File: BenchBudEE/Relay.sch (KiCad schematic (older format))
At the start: 10 parts

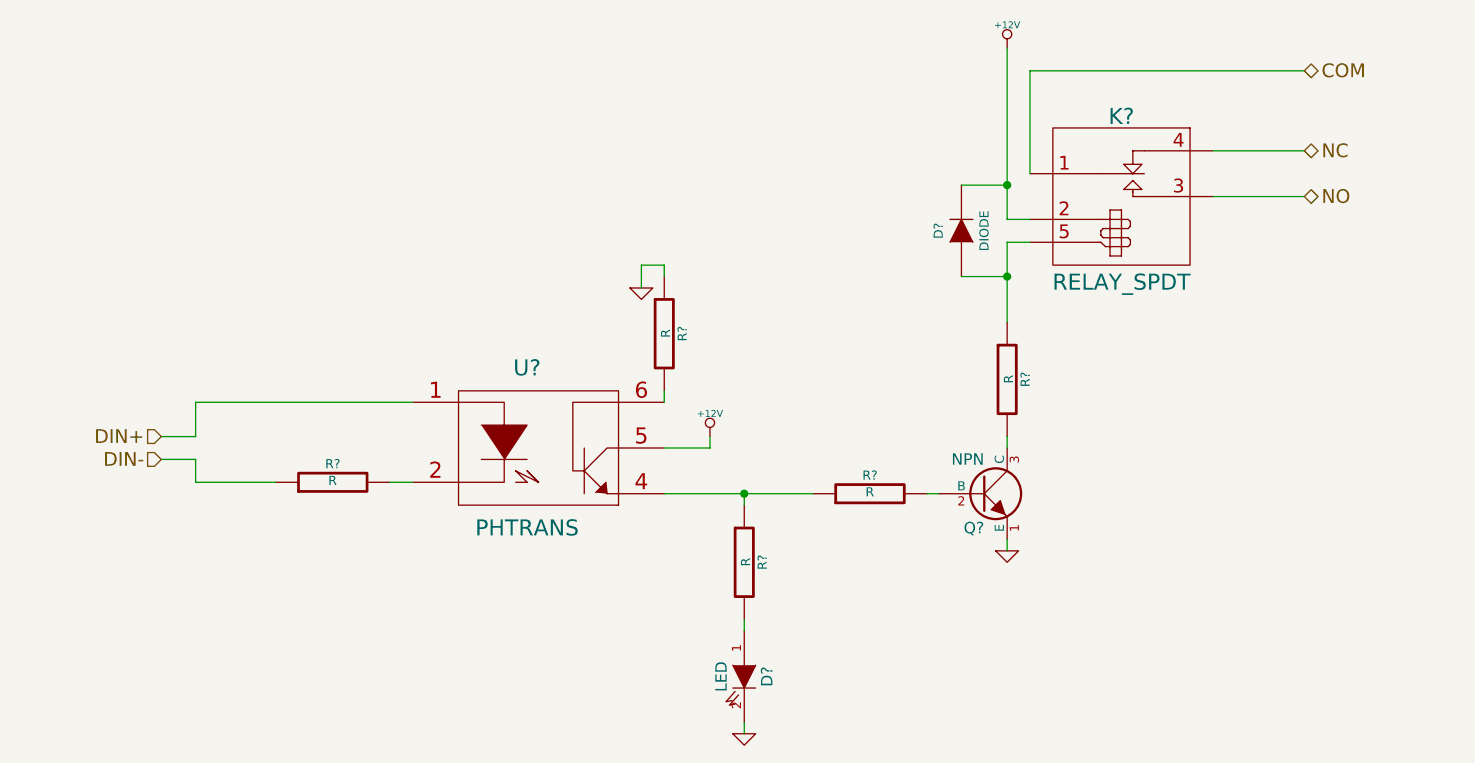
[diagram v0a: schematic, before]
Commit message: Completing schematics from week 3 videos.
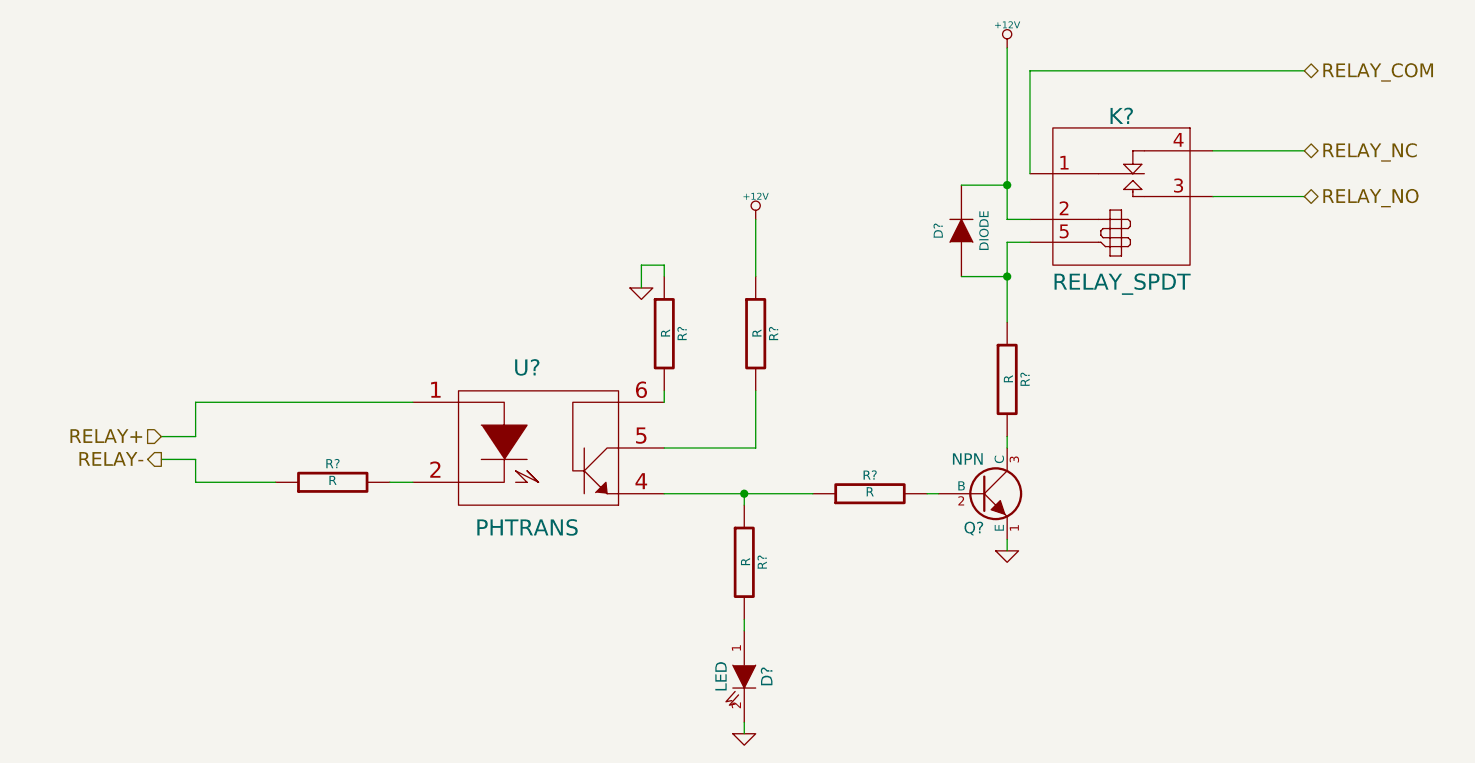
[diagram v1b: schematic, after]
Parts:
- added R?: R, ~, symbol R
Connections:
- net +12V: now also R?.1; no longer U?.5
- net COM renamed RELAY_COM
- net DIN+ renamed RELAY+
- net DIN- renamed RELAY-
- net NC renamed RELAY_NC
- net NO renamed RELAY_NO
- new net: R?.2, U?.5
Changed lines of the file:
@@
 LIBS:relay_spdt
 LIBS:5566-20A
+LIBS:AP5726
+LIBS:arduino
 LIBS:BenchBudEE-cache
 EELAYER 27 0
@@
 $Descr A4 11693 8268
 encoding utf-8
-Sheet 4 9
+Sheet 3 9
 Title ""
-Date "13 feb 2014"
+Date "24 feb 2014"
 Rev ""
 Comp ""
@@
 $EndDescr
 Text HLabel 2900 4350 0    60   Input ~ 0
-DIN+
-Text HLabel 2900 4450 0    60   Input ~ 0
-DIN-
+RELAY+
+Text HLabel 2900 4450 0    60   Output ~ 0
+RELAY-
 Text HLabel 7900 3100 2    60   BiDi ~ 0
-NC
+RELAY_NC
 Text HLabel 7900 3300 2    60   BiDi ~ 0
-NO
+RELAY_NO
 $Comp
 L RELAY_SPDT K?
@@
 $EndComp
 Text HLabel 7900 2750 2    60   BiDi ~ 0
-COM
+RELAY_COM
 Wire Wire Line
 	7500 3100 7900 3100
@@
 L +12V #PWR?
 U 1 1 52F83D30
-P 5300 4350
-F 0 "#PWR?" H 5300 4300 20  0001 C CNN
-F 1 "+12V" H 5300 4450 30  0000 C CNN
-F 2 "" H 5300 4350 60  0000 C CNN
-F 3 "" H 5300 4350 60  0000 C CNN
-	1    5300 4350
-	1    0    0    -1
-$EndComp
-Wire Wire Line
-	5100 4400 5300 4400
+P 5500 3400
+F 0 "#PWR?" H 5500 3350 20  0001 C CNN
+F 1 "+12V" H 5500 3500 30  0000 C CNN
+F 2 "" H 5500 3400 60  0000 C CNN
+F 3 "" H 5500 3400 60  0000 C CNN
+	1    5500 3400
+	1    0    0    -1
+$EndComp
 $Comp
 L GND #PWR?
@@
 Wire Wire Line
 	5100 4200 5100 4150
-Wire Wire Line
-	5300 4400 5300 4350
 $Comp
 L DIODE D?
@@
 	6400 3650 6600 3650
 Connection ~ 6600 3650
+$Comp
+L R R?
+U 1 1 530982E3
+P 5500 3900
+F 0 "R?" V 5580 3900 40  0000 C CNN
+F 1 "R" V 5507 3901 40  0000 C CNN
+F 2 "~" V 5430 3900 30  0000 C CNN
+F 3 "~" H 5500 3900 30  0000 C CNN
+	1    5500 3900
+	1    0    0    -1
+$EndComp
+Wire Wire Line
+	5500 3400 5500 3650
+Wire Wire Line
+	5500 4150 5500 4400
+Wire Wire Line
+	5500 4400 5100 4400
 $EndSCHEMATC

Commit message: checking in all my local changes before syncing to chris's repo.
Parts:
- removed R?: R, ~, symbol R
- removed U?: PHTRANS, ~, symbol PHTRANS
- added U1: LVT-816S, symbol OPTO-TRANSISTOR4
- D1: renamed from D?; value LED -> Q971-KN-1
- D2: renamed from D?; value DIODE -> B130-13-F
- Q1: renamed from Q?; value NPN -> MMBT3904
- gave numbers to parts that had none: 6
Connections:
- net RELAY+: now also U1.1 (A)
- net at R2.1, R4.1: now also U1.3 (E)
- net at R1.2: now also U1.2 (K)
- net at R3.2: now also U1.4 (C)
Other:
- moved on the sheet: R1, R3
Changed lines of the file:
@@
 Sheet 3 9
 Title ""
-Date "24 feb 2014"
+Date "2 mar 2014"
 Rev ""
 Comp ""
@@
 Comment4 ""
 $EndDescr
-Text HLabel 2900 4350 0    60   Input ~ 0
+Text HLabel 2750 4400 0    60   Input ~ 0
 RELAY+
-Text HLabel 2900 4450 0    60   Output ~ 0
+Text HLabel 2750 4500 0    60   Output ~ 0
 RELAY-
 Text HLabel 7900 3100 2    60   BiDi ~ 0
@@
 RELAY_NO
 $Comp
-L RELAY_SPDT K?
+L RELAY_SPDT K1
 U 1 1 52F83A2E
 P 7100 3150
-F 0 "K?" H 7100 3350 70  0000 C CNN
+F 0 "K1" H 7100 3350 70  0000 C CNN
 F 1 "RELAY_SPDT" H 7100 2625 70  0000 C CNN
 F 2 "~" H 7100 3150 60  0000 C CNN
@@
 	7500 3300 7900 3300
 $Comp
-L NPN Q?
+L NPN Q1
 U 1 1 52F83A84
 P 6500 4600
-F 0 "Q?" H 6500 4450 50  0000 R CNN
-F 1 "NPN" H 6500 4750 50  0000 R CNN
+F 0 "Q1" H 6500 4450 50  0000 R CNN
+F 1 "MMBT3904" H 6500 4750 50  0000 R CNN
 F 2 "~" H 6500 4600 60  0000 C CNN
 F 3 "~" H 6500 4600 60  0000 C CNN
@@
 $EndComp
 $Comp
-L R R?
+L R R5
 U 1 1 52F83A94
 P 6600 4100
-F 0 "R?" V 6680 4100 40  0000 C CNN
+F 0 "R5" V 6680 4100 40  0000 C CNN
 F 1 "R" V 6607 4101 40  0000 C CNN
 F 2 "~" V 6530 4100 30  0000 C CNN
@@
 	6600 3500 6700 3500
 $Comp
-L +12V #PWR?
+L +12V #PWR9
 U 1 1 52F83AA0
 P 6600 2650
-F 0 "#PWR?" H 6600 2600 20  0001 C CNN
+F 0 "#PWR9" H 6600 2600 20  0001 C CNN
 F 1 "+12V" H 6600 2750 30  0000 C CNN
 F 2 "" H 6600 2650 60  0000 C CNN
@@
 $EndComp
 $Comp
-L GND #PWR?
+L GND #PWR10
 U 1 1 52F83ADF
 P 6600 4850
-F 0 "#PWR?" H 6600 4850 30  0001 C CNN
+F 0 "#PWR10" H 6600 4850 30  0001 C CNN
 F 1 "GND" H 6600 4780 30  0001 C CNN
 F 2 "" H 6600 4850 60  0000 C CNN
@@
 $EndComp
 $Comp
-L R R?
+L R R4
 U 1 1 52F83AF5
 P 6000 4600
-F 0 "R?" V 6080 4600 40  0000 C CNN
+F 0 "R4" V 6080 4600 40  0000 C CNN
 F 1 "R" V 6007 4601 40  0000 C CNN
 F 2 "~" V 5930 4600 30  0000 C CNN
@@
 	0    -1   -1   0
 $EndComp
-$Comp
-L PHTRANS U?
-U 1 1 52F83B05
-P 4550 4400
-F 0 "U?" H 4500 4750 70  0000 C CNN
-F 1 "PHTRANS" H 4500 4050 70  0000 C CNN
-F 2 "~" H 4550 4400 60  0000 C CNN
-F 3 "~" H 4550 4400 60  0000 C CNN
-	1    4550 4400
-	1    0    0    -1
-$EndComp
 Wire Wire Line
 	5100 4600 5750 4600
 $Comp
-L LED D?
+L LED D1
 U 1 1 52F83B20
 P 5450 5400
-F 0 "D?" H 5450 5500 50  0000 C CNN
-F 1 "LED" H 5450 5300 50  0000 C CNN
+F 0 "D1" H 5450 5500 50  0000 C CNN
+F 1 "Q971-KN-1" H 5450 5300 50  0000 C CNN
 F 2 "~" H 5450 5400 60  0000 C CNN
 F 3 "~" H 5450 5400 60  0000 C CNN
@@
 $EndComp
 $Comp
-L R R?
+L R R2
 U 1 1 52F83B3F
 P 5450 4900
-F 0 "R?" V 5530 4900 40  0000 C CNN
+F 0 "R2" V 5530 4900 40  0000 C CNN
 F 1 "R" V 5457 4901 40  0000 C CNN
 F 2 "~" V 5380 4900 30  0000 C CNN
@@
 $EndComp
 $Comp
-L GND #PWR?
+L GND #PWR7
 U 1 1 52F83B5E
 P 5450 5650
-F 0 "#PWR?" H 5450 5650 30  0001 C CNN
+F 0 "#PWR7" H 5450 5650 30  0001 C CNN
 F 1 "GND" H 5450 5580 30  0001 C CNN
 F 2 "" H 5450 5650 60  0000 C CNN
@@
 $EndComp
 $Comp
-L R R?
+L R R1
 U 1 1 52F83B95
-P 3650 4550
-F 0 "R?" V 3730 4550 40  0000 C CNN
-F 1 "R" V 3657 4551 40  0000 C CNN
-F 2 "~" V 3580 4550 30  0000 C CNN
-F 3 "~" H 3650 4550 30  0000 C CNN
-	1    3650 4550
+P 3500 4600
+F 0 "R1" V 3580 4600 40  0000 C CNN
+F 1 "R" V 3507 4601 40  0000 C CNN
+F 2 "~" V 3430 4600 30  0000 C CNN
+F 3 "~" H 3500 4600 30  0000 C CNN
+	1    3500 4600
 	0    -1   -1   0
 $EndComp
 Wire Wire Line
-	3900 4550 4000 4550
-Wire Wire Line
-	2900 4350 3050 4350
-Wire Wire Line
-	3050 4350 3050 4200
-Wire Wire Line
-	3050 4200 4000 4200
-Wire Wire Line
-	3400 4550 3050 4550
-Wire Wire Line
-	3050 4550 3050 4450
-Wire Wire Line
-	3050 4450 2900 4450
+	3750 4600 3850 4600
+Wire Wire Line
+	2750 4400 2900 4400
+Wire Wire Line
+	3250 4600 2900 4600
+Wire Wire Line
+	2900 4600 2900 4500
+Wire Wire Line
+	2900 4500 2750 4500
 Wire Wire Line
 	6600 4350 6600 4400
@@
 	5450 5600 5450 5650
 $Comp
-L +12V #PWR?
+L +12V #PWR8
 U 1 1 52F83D30
-P 5500 3400
-F 0 "#PWR?" H 5500 3350 20  0001 C CNN
-F 1 "+12V" H 5500 3500 30  0000 C CNN
-F 2 "" H 5500 3400 60  0000 C CNN
-F 3 "" H 5500 3400 60  0000 C CNN
-	1    5500 3400
-	1    0    0    -1
-$EndComp
-$Comp
-L GND #PWR?
-U 1 1 52F83D4D
-P 5000 3700
-F 0 "#PWR?" H 5000 3700 30  0001 C CNN
-F 1 "GND" H 5000 3630 30  0001 C CNN
-F 2 "" H 5000 3700 60  0000 C CNN
-F 3 "" H 5000 3700 60  0000 C CNN
-	1    5000 3700
-	1    0    0    -1
-$EndComp
-$Comp
-L R R?
-U 1 1 52F83D6E
-P 5100 3900
-F 0 "R?" V 5180 3900 40  0000 C CNN
-F 1 "R" V 5107 3901 40  0000 C CNN
-F 2 "~" V 5030 3900 30  0000 C CNN
-F 3 "~" H 5100 3900 30  0000 C CNN
-	1    5100 3900
-	1    0    0    -1
-$EndComp
-Wire Wire Line
-	5100 3650 5100 3600
-Wire Wire Line
-	5100 3600 5000 3600
-Wire Wire Line
-	5000 3600 5000 3700
-Wire Wire Line
-	5100 4200 5100 4150
-$Comp
-L DIODE D?
+P 5500 3300
+F 0 "#PWR8" H 5500 3250 20  0001 C CNN
+F 1 "+12V" H 5500 3400 30  0000 C CNN
+F 2 "" H 5500 3300 60  0000 C CNN
+F 3 "" H 5500 3300 60  0000 C CNN
+	1    5500 3300
+	1    0    0    -1
+$EndComp
+$Comp
+L DIODE D2
 U 1 1 52F83F01
 P 6400 3450
-F 0 "D?" H 6400 3550 40  0000 C CNN
-F 1 "DIODE" H 6400 3350 40  0000 C CNN
+F 0 "D2" H 6400 3550 40  0000 C CNN
+F 1 "B130-13-F" H 6400 3350 40  0000 C CNN
 F 2 "~" H 6400 3450 60  0000 C CNN
 F 3 "~" H 6400 3450 60  0000 C CNN
@@
 	6700 2750 7900 2750
 Wire Wire Line
-	6700 3400 6600 3400
-Wire Wire Line
-	6600 3400 6600 2650
+	6600 3400 6700 3400
+Wire Wire Line
+	6600 2650 6600 3400
 Wire Wire Line
 	6400 3250 6600 3250
@@
 Connection ~ 6600 3650
 $Comp
-L R R?
+L R R3
 U 1 1 530982E3
-P 5500 3900
-F 0 "R?" V 5580 3900 40  0000 C CNN
-F 1 "R" V 5507 3901 40  0000 C CNN
-F 2 "~" V 5430 3900 30  0000 C CNN
-F 3 "~" H 5500 3900 30  0000 C CNN
-	1    5500 3900
-	1    0    0    -1
-$EndComp
-Wire Wire Line
-	5500 3400 5500 3650
-Wire Wire Line
-	5500 4150 5500 4400
-Wire Wire Line
-	5500 4400 5100 4400
+P 5500 3800
+F 0 "R3" V 5580 3800 40  0000 C CNN
+F 1 "R" V 5507 3801 40  0000 C CNN
+F 2 "~" V 5430 3800 30  0000 C CNN
+F 3 "~" H 5500 3800 30  0000 C CNN
+	1    5500 3800
+	1    0    0    -1
+$EndComp
+Wire Wire Line
+	5500 3300 5500 3550
+Wire Wire Line
+	5500 4050 5500 4300
+Wire Wire Line
+	5500 4300 5100 4300
+$Comp
+L OPTO-TRANSISTOR4 U1
+U 1 1 531261FF
+P 4500 4450
+F 0 "U1" H 4700 4700 60  0000 C CNN
+F 1 "LVT-816S" H 4500 4200 60  0000 C CNN
+F 2 "" H 4500 4450 60  0000 C CNN
+F 3 "" H 4500 4450 60  0000 C CNN
+	1    4500 4450
+	1    0    0    -1
+$EndComp
+Wire Wire Line
+	3850 4300 2900 4300
+Wire Wire Line
+	2900 4300 2900 4400
 $EndSCHEMATC
